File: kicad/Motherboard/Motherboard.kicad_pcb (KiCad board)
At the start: 2 copper layers, 64 parts, among them J1 USB_C_Receptacle_USB2.0, J2 Conn_01x16_Pin, J3 Conn_01x16_Pin, J4 Conn_01x16_Pin, J5 Conn_01x02_Pin, J6 Conn_01x04_Pin, J7 Conn_01x04_Pin, J8 Conn_01x16_Pin, J9 Conn_01x02_Pin, Q1 DMN3404L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

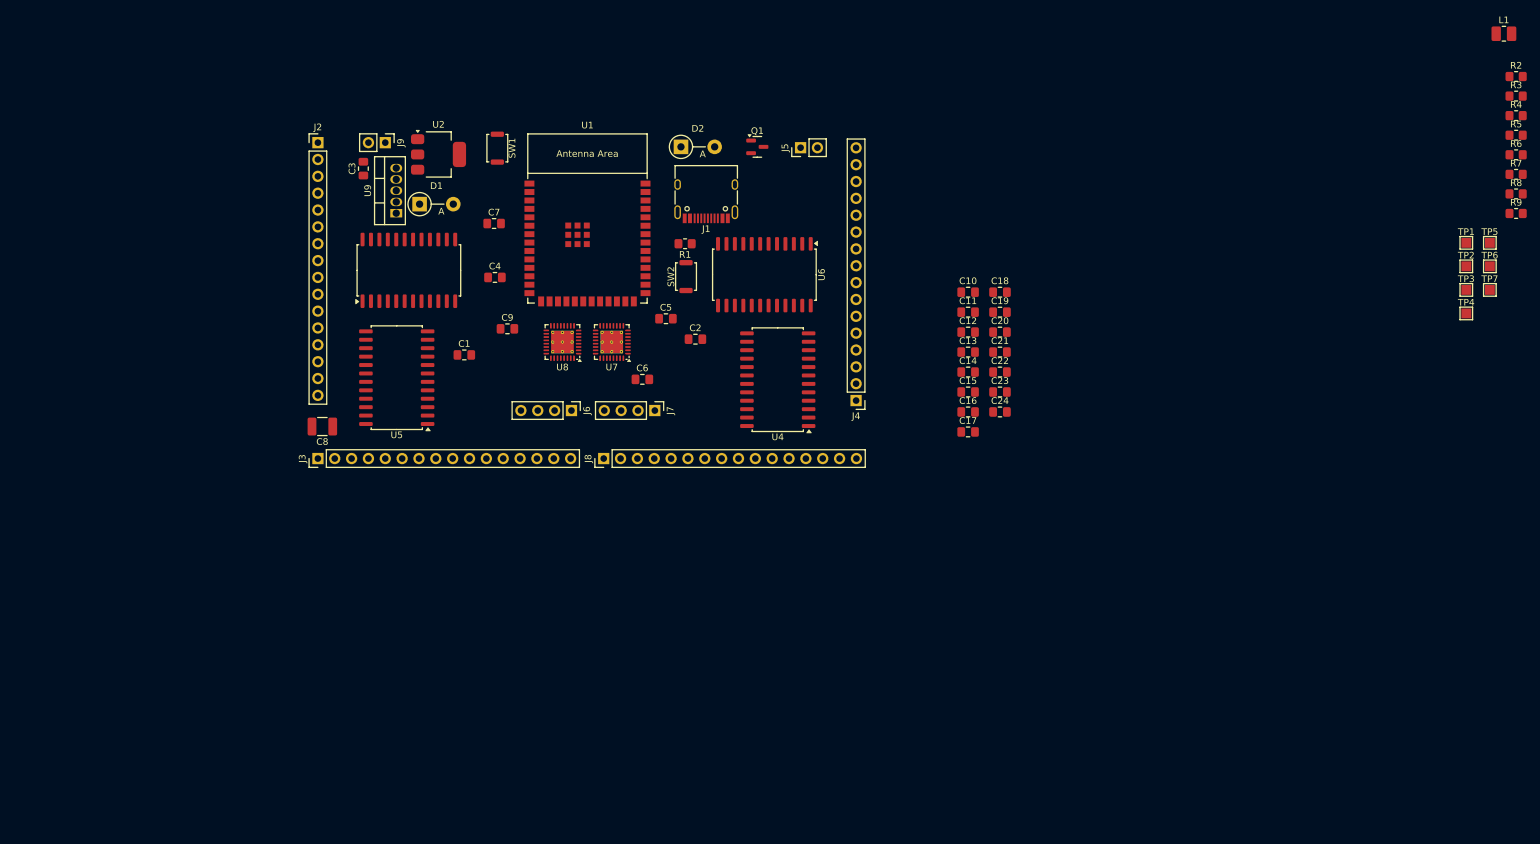
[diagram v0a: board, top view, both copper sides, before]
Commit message: Almost done - going to do a few more changes before I run the auto connector
We may want to manually add them tho cus apple is going to look at it...
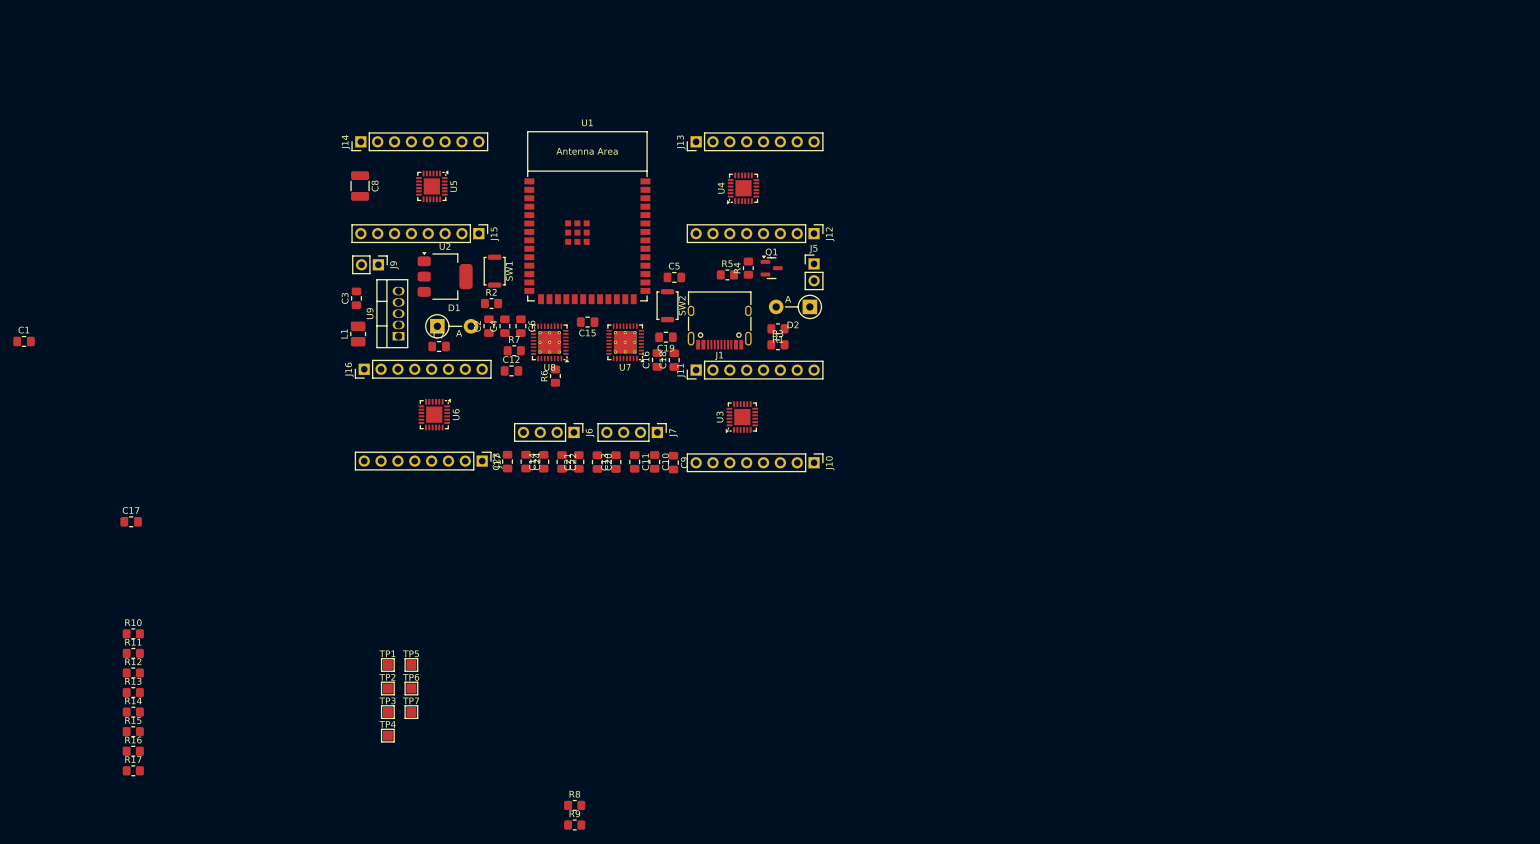
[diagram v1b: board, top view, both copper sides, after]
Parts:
- removed J2, J3, J4, J8: Conn_01x16_Pin, Connector_PinHeader_2.54mm:PinHeader_1x16_P2.54mm_Vertical
- added J10: Conn_01x08_Pin, Connector_PinHeader_2.54mm:PinHeader_1x08_P2.54mm_Vertical, F.Cu at (154.3, 129.5)
- added J11: Conn_01x08_Pin, Connector_PinHeader_2.54mm:PinHeader_1x08_P2.54mm_Vertical, F.Cu at (136.5, 115.6)
- added J12: Conn_01x08_Pin, Connector_PinHeader_2.54mm:PinHeader_1x08_P2.54mm_Vertical, F.Cu at (154.3, 95.0)
- added J13: Conn_01x08_Pin, Connector_PinHeader_2.54mm:PinHeader_1x08_P2.54mm_Vertical, F.Cu at (136.5, 81.2)
- added J14: Conn_01x08_Pin, Connector_PinHeader_2.54mm:PinHeader_1x08_P2.54mm_Vertical, F.Cu at (86.0, 81.2)
- added J15: Conn_01x08_Pin, Connector_PinHeader_2.54mm:PinHeader_1x08_P2.54mm_Vertical, F.Cu at (103.8, 95.0)
- added J16: Conn_01x08_Pin, Connector_PinHeader_2.54mm:PinHeader_1x08_P2.54mm_Vertical, F.Cu at (86.5, 115.4)
- added J17: Conn_01x08_Pin, Connector_PinHeader_2.54mm:PinHeader_1x08_P2.54mm_Vertical, F.Cu at (104.3, 129.3)
- added R10: 10k, Resistor_SMD:R_0805_2012Metric_Pad1.20x1.40mm_HandSolder, F.Cu at (51.7, 155.3)
- added R11: 10k, Resistor_SMD:R_0805_2012Metric_Pad1.20x1.40mm_HandSolder, F.Cu at (51.7, 158.3)
- added R12: 10k, Resistor_SMD:R_0805_2012Metric_Pad1.20x1.40mm_HandSolder, F.Cu at (51.7, 161.2)
- added R13: 10k, Resistor_SMD:R_0805_2012Metric_Pad1.20x1.40mm_HandSolder, F.Cu at (51.7, 164.2)
- added R14: 10k, Resistor_SMD:R_0805_2012Metric_Pad1.20x1.40mm_HandSolder, F.Cu at (51.7, 167.1)
- added R15: 10k, Resistor_SMD:R_0805_2012Metric_Pad1.20x1.40mm_HandSolder, F.Cu at (51.7, 170.1)
- added R16: 10k, Resistor_SMD:R_0805_2012Metric_Pad1.20x1.40mm_HandSolder, F.Cu at (51.7, 173.0)
- added R17: 10k, Resistor_SMD:R_0805_2012Metric_Pad1.20x1.40mm_HandSolder, F.Cu at (51.7, 176.0)
- U3, U4, U5, U6: value CD74HC4067M -> TCA9535RTWR; footprint Package_SO:SOIC-24W_7.5x15.4mm_P1.27mm -> Package_DFN_QFN:WQFN-24-1EP_4x4mm_P0.5mm_EP2.45x2.45mm
- moved L1 178.6 mm to (85.6, 110.1), turned to 90 degrees
- moved TP5 174.6 mm to (93.6, 160.0)
- moved TP6 174.6 mm to (93.6, 163.6)
- moved TP7 174.6 mm to (93.6, 167.1)
- moved TP1 174.6 mm to (90.0, 160.0)
- moved TP2 174.6 mm to (90.0, 163.6)
- moved TP3 174.6 mm to (90.0, 167.1)
- moved TP4 174.6 mm to (90.0, 170.7)
- moved R8 169.2 mm to (118.2, 181.2)
- moved R9 169.2 mm to (118.2, 184.2)
- moved R2 158.2 mm to (105.7, 105.5)
- moved R7 153.4 mm to (109.1, 112.6)
- moved R6 148.6 mm to (115.3, 116.5), turned to 90 degrees
- moved C17 126.9 mm to (51.3, 138.4)
- moved R5 120.8 mm to (141.2, 101.2)
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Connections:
- C2 pad 2: +3.3V -> SDA
- C4 pad 2: +3.3V -> SDA
- C6 pad 1: +3.3V -> SDA
- R2 pad 1: +3.3V -> SDA
- TP5 pad 1: +3.3V -> SDA
- U1 pad 12: COM1 -> unconnected-(U1-GPIO8/TOUCH8/ADC1_CH7-Pad12)
- U1 pad 15: bit2 -> unconnected-(U1-GPIO3/TOUCH3/ADC1_CH2-Pad15)
- U1 pad 17: EN2 -> unconnected-(U1-GPIO9/TOUCH9/ADC1_CH8/FSPIHD-Pad17)
- U1 pad 18: COM2 -> unconnected-(U1-GPIO10/TOUCH10/ADC1_CH9/FSPICS0/FSPIIO4-Pad18)
- U1 pad 19: EN3 -> unconnected-(U1-GPIO11/TOUCH11/ADC2_CH0/FSPID/FSPIIO5-Pad19)
- U1 pad 2: +3.3V -> SDA
- U1 pad 20: COM3 -> unconnected-(U1-GPIO12/TOUCH12/ADC2_CH1/FSPICLK/FSPIIO6-Pad20)
- U1 pad 38: bit1 -> SCL
- U1 pad 39: bit0 -> SDA
- U1 pad 4: bit3 -> unconnected-(U1-GPIO4/TOUCH4/ADC1_CH3-Pad4)
- U1 pad 5: EN0 -> unconnected-(U1-GPIO5/TOUCH5/ADC1_CH4-Pad5)
- U1 pad 6: COM0 -> unconnected-(U1-GPIO6/TOUCH6/ADC1_CH5-Pad6)
- U1 pad 7: EN1 -> unconnected-(U1-GPIO7/TOUCH7/ADC1_CH6-Pad7)
- U2 pad 2: +3.3V -> SDA
- U3 pad 1: COM0 -> Net-(J10-Pin_8)
- U3 pad 10: bit0 -> Net-(J11-Pin_8)
- U3 pad 11: bit1 -> Net-(J11-Pin_7)
- U3 pad 12: GND -> Net-(J11-Pin_6)
- U3 pad 13: bit3 -> Net-(J11-Pin_5)
- U3 pad 14: bit2 -> Net-(J11-Pin_4)
- U3 pad 15: EN0 -> Net-(J11-Pin_3)
- U3 pad 18: Net-(J2-Pin_3) -> GND
- U3 pad 19: Net-(J2-Pin_4) -> SCL
- U3 pad 20: Net-(J2-Pin_5) -> SDA
- U3 pad 21: Net-(J2-Pin_6) -> SDA
- U3 pad 22: Net-(J2-Pin_7) -> unconnected-(U3-~{INT}-Pad22)
- U3 pad 23: Net-(J2-Pin_8) -> GND
- U3 pad 24: +5V -> GND
- U3 pad 9: Net-(J2-Pin_16) -> GND
- U4 pad 1: COM1 -> Net-(J12-Pin_8)
- U4 pad 10: bit0 -> Net-(J13-Pin_8)
- U4 pad 11: bit1 -> Net-(J13-Pin_7)
- U4 pad 12: GND -> Net-(J13-Pin_6)
- U4 pad 13: bit3 -> Net-(J13-Pin_5)
- U4 pad 14: bit2 -> Net-(J13-Pin_4)
- U4 pad 15: EN1 -> Net-(J13-Pin_3)
- U4 pad 18: Net-(J8-Pin_3) -> GND
- U4 pad 19: Net-(J8-Pin_4) -> SCL
- U4 pad 20: Net-(J8-Pin_5) -> SDA
- U4 pad 21: Net-(J8-Pin_6) -> SDA
- U4 pad 22: Net-(J8-Pin_7) -> unconnected-(U4-~{INT}-Pad22)
- U4 pad 23: Net-(J8-Pin_8) -> GND
- U4 pad 24: +5V -> SDA
- U4 pad 9: Net-(J8-Pin_16) -> GND
- U5 pad 1: COM2 -> Net-(J14-Pin_8)
- U5 pad 10: bit0 -> Net-(J15-Pin_8)
- U5 pad 11: bit1 -> Net-(J15-Pin_7)
- U5 pad 12: GND -> Net-(J15-Pin_6)
- U5 pad 13: bit3 -> Net-(J15-Pin_5)
- U5 pad 14: bit2 -> Net-(J15-Pin_4)
- U5 pad 15: EN2 -> Net-(J15-Pin_3)
- U5 pad 18: Net-(J3-Pin_3) -> GND
- U5 pad 19: Net-(J3-Pin_4) -> SCL
- U5 pad 20: Net-(J3-Pin_5) -> SDA
- U5 pad 21: Net-(J3-Pin_6) -> SDA
- U5 pad 22: Net-(J3-Pin_7) -> unconnected-(U5-~{INT}-Pad22)
- U5 pad 23: Net-(J3-Pin_8) -> SDA
- U5 pad 24: +5V -> GND
- U5 pad 9: Net-(J3-Pin_16) -> GND
- U6 pad 1: COM3 -> Net-(J16-Pin_8)
- U6 pad 10: bit0 -> Net-(J17-Pin_8)
- U6 pad 11: bit1 -> Net-(J17-Pin_7)
- U6 pad 12: GND -> Net-(J17-Pin_6)
- U6 pad 13: bit3 -> Net-(J17-Pin_5)
- U6 pad 14: bit2 -> Net-(J17-Pin_4)
- U6 pad 15: EN3 -> Net-(J17-Pin_3)
- U6 pad 18: Net-(J4-Pin_3) -> SDA
- U6 pad 19: Net-(J4-Pin_4) -> SCL
- U6 pad 20: Net-(J4-Pin_5) -> SDA
- U6 pad 21: Net-(J4-Pin_6) -> SDA
- U6 pad 22: Net-(J4-Pin_7) -> unconnected-(U6-~{INT}-Pad22)
- U6 pad 23: Net-(J4-Pin_8) -> GND
- U6 pad 24: +5V -> GND
- U6 pad 9: Net-(J4-Pin_16) -> GND
- U7 pad 15: +3.3V -> SDA
- U8 pad 15: +3.3V -> SDA

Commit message: updated layout
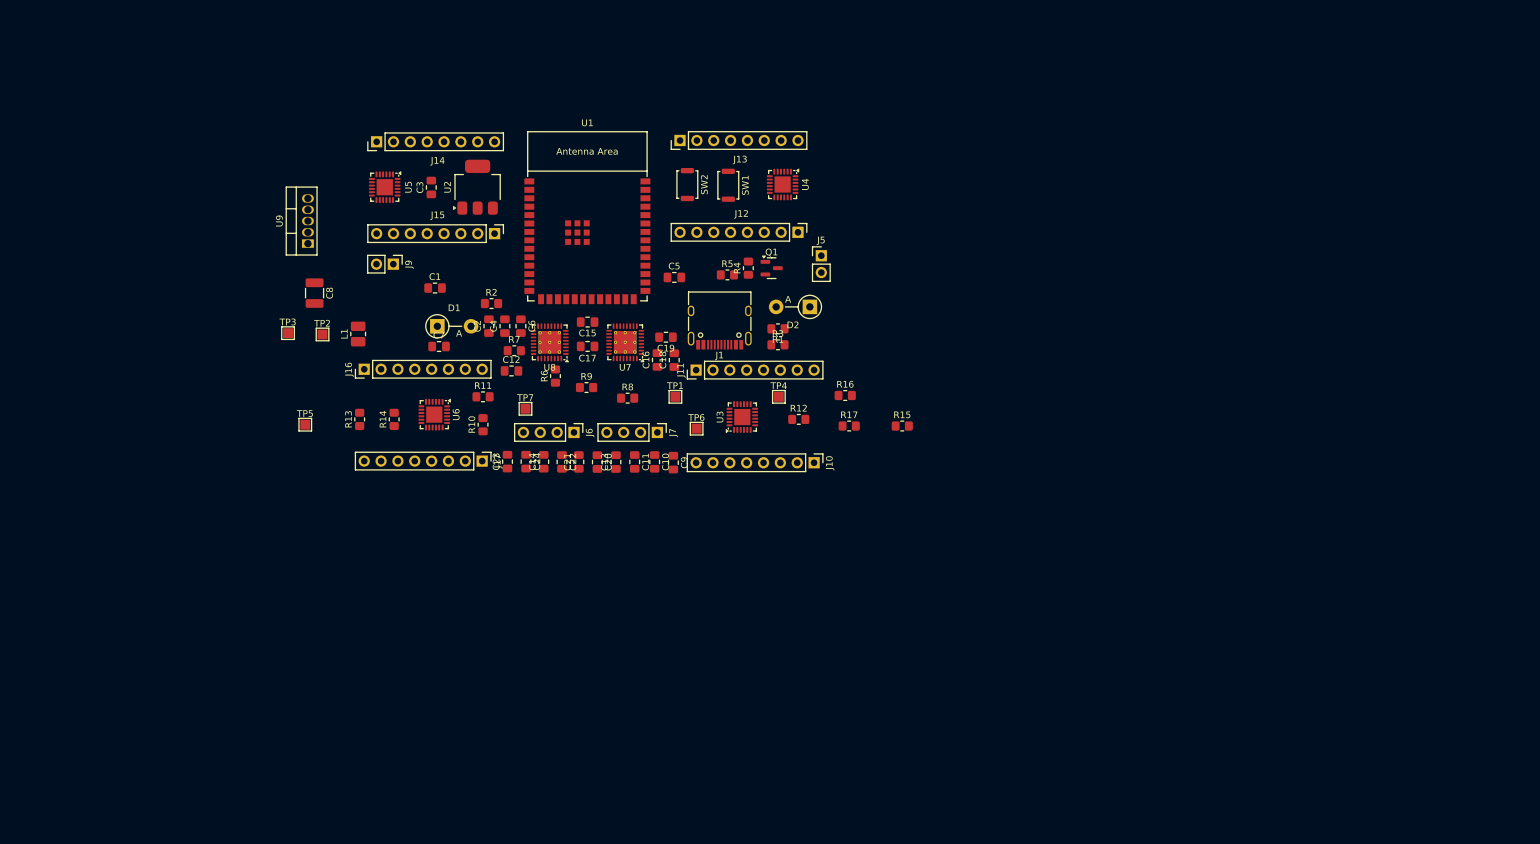
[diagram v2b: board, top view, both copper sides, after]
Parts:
- moved R15 124.8 mm to (167.6, 124.0)
- moved R16 120.0 mm to (159.0, 119.4)
- moved R17 119.8 mm to (159.6, 124.0)
- moved R12 107.4 mm to (152.0, 123.0)
- moved TP4 78.0 mm to (149.0, 119.6)
- moved C17 73.7 mm to (120.2, 112.0)
- moved R9 66.0 mm to (120.0, 118.2)
- moved R11 65.4 mm to (104.4, 119.6)
- moved C1 62.5 mm to (97.2, 103.2)
- moved R8 61.9 mm to (126.2, 119.8)
- moved R10 61.4 mm to (104.4, 123.8), turned to 90 degrees
- moved TP1 59.3 mm to (133.4, 119.6)
- moved R14 59.1 mm to (91.0, 123.0), turned to 90 degrees
- moved TP3 59.1 mm to (75.0, 110.0)
- moved TP6 58.2 mm to (136.6, 124.4)
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
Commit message: Gode
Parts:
- moved TP4 78.0 mm to (90.0, 170.7)
- moved TP5 69.4 mm to (132.2, 81.0)
- moved TP6 51.0 mm to (92.3, 99.1)
- moved R15 50.3 mm to (117.3, 125.1), turned to -90 degrees
- moved R17 48.2 mm to (111.4, 125.1), turned to -90 degrees
- moved R16 45.0 mm to (114.4, 125.1), turned to -90 degrees
- moved R10 44.8 mm to (132.2, 88.7), turned to -90 degrees
- moved TP1 39.6 mm to (94.5, 112.0)
- moved R13 37.5 mm to (123.2, 125.1), turned to -90 degrees
- moved SW1 36.3 mm to (105.1, 86.2), turned to 0 degrees
- moved R14 29.3 mm to (120.3, 125.1), turned to -90 degrees
- moved R12 25.9 mm to (126.2, 125.1), turned to -90 degrees
- moved TP3 25.7 mm to (73.5, 135.6)
- moved R11 25.3 mm to (129.1, 125.1), turned to -90 degrees
- moved C3 20.2 mm to (85.3, 104.8)
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
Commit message: re-render layout
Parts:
- removed TP3: BeforeEM_TestPoint, TestPoint:TestPoint_Pad_1.5x1.5mm
- moved TP4 48.8 mm to (105.4, 124.4)
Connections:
- C1 pad 1: GND -> +3.3V
- C10 pad 2: GND -> +3.3V
- C11 pad 2: GND -> +3.3V
- C13 pad 1: GND -> +3.3V
- C14 pad 1: GND -> +3.3V
- C15 pad 1: GND -> +3.3V
- C19 pad 1: GND -> +3.3V
- C2 pad 1: GND -> +3.3V
- C2 pad 2: SDA -> +3.3V
- C20 pad 2: GND -> +3.3V
- C21 pad 1: GND -> +3.3V
- C22 pad 2: GND -> +3.3V
- C23 pad 1: GND -> +3.3V
- C24 pad 2: GND -> +3.3V
- C3 pad 2: GND -> +3.3V
- C4 pad 1: GND -> +3.3V
- C4 pad 2: SDA -> +3.3V
- C5 pad 2: GND -> +3.3V
- C6 pad 1: SDA -> +3.3V
- C6 pad 2: GND -> +3.3V
- C7 pad 2: GND -> +3.3V
- C8 pad 2: GND -> +3.3V
- C9 pad 2: GND -> +3.3V
- D1 pad 2: GND -> +3.3V
- J1 pad A1: GND -> +3.3V
- J1 pad A12: GND -> +3.3V
- J1 pad B1: GND -> +3.3V
- J1 pad B12: GND -> +3.3V
- J1 pad S1: GND -> +3.3V
- J9 pad 2: GND -> +3.3V
- Q1 pad 2: GND -> +3.3V
- R1 pad 1: GND -> +3.3V
- R10 pad 1: SDA -> +3.3V
- R11 pad 1: SDA -> +3.3V
- R12 pad 1: SDA -> +3.3V
- R12 pad 2: SDA -> SCL
- R13 pad 1: SDA -> +3.3V
- R13 pad 2: SDA -> SCL
- R14 pad 1: SDA -> +3.3V
- R15 pad 1: SDA -> +3.3V
- R15 pad 2: SDA -> SCL
- R16 pad 1: SDA -> +3.3V
- R17 pad 1: SDA -> +3.3V
- R17 pad 2: SDA -> SCL
- R2 pad 1: SDA -> +3.3V
- R3 pad 2: GND -> +3.3V
- R5 pad 1: GND -> +3.3V
- R6 pad 1: GND -> +3.3V
- R7 pad 1: GND -> +3.3V
- R8 pad 1: GND -> +3.3V
- R9 pad 1: GND -> +3.3V
- SW1 pad 1: GND -> +3.3V
- SW2 pad 2: GND -> +3.3V
- TP4 pad 1: GND -> +3.3V
- TP5 pad 1: SDA -> +3.3V
- U1 pad 1: GND -> +3.3V
- U1 pad 10: STEP_1 -> unconnected-(U1-GPIO17/U1TXD/ADC2_CH6/DAC_1-Pad10)
- U1 pad 11: UART_1 -> unconnected-(U1-GPIO18/U1RXD/ADC2_CH7/DAC_2/CLK_OUT3-Pad11)
- U1 pad 13: unconnected-(U1-GPIO19/U1RTS/ADC2_CH8/CLK_OUT2/USB_D--Pad13) -> /D-
- U1 pad 14: unconnected-(U1-GPIO20/U1CTS/ADC2_CH9/CLK_OUT1/USB_D+-Pad14) -> /D+
- U1 pad 15: unconnected-(U1-GPIO3/TOUCH3/ADC1_CH2-Pad15) -> STEP_1
- U1 pad 18: unconnected-(U1-GPIO10/TOUCH10/ADC1_CH9/FSPICS0/FSPIIO4-Pad18) -> MAGCT
- U1 pad 2: SDA -> +3.3V
- U1 pad 21: ENN_1 -> unconnected-(U1-GPIO13/TOUCH13/ADC2_CH2/FSPIQ/FSPIIO7-Pad21)
- U1 pad 22: DIR_1 -> unconnected-(U1-GPIO14/TOUCH14/ADC2_CH3/FSPIWP/FSPIDQS-Pad22)
- U1 pad 23: ENN_2 -> unconnected-(U1-GPIO21-Pad23)
- U1 pad 24: DIR_2 -> SCL
- U1 pad 25: STEP_2 -> SCL
- U1 pad 28: UART_2 -> unconnected-(U1-SPIIO6/GPIO35/FSPID-Pad28)
- U1 pad 29: MAGCT -> unconnected-(U1-SPIIO7/GPIO36/FSPICLK-Pad29)
- U1 pad 36: unconnected-(U1-U0RXD/GPIO44/CLK_OUT2-Pad36) -> UART_1
- U1 pad 37: unconnected-(U1-U0TXD/GPIO43/CLK_OUT1-Pad37) -> UART_2
- U1 pad 38: SCL -> DIR_1
- U1 pad 39: SDA -> ENN_1
- U1 pad 4: unconnected-(U1-GPIO4/TOUCH4/ADC1_CH3-Pad4) -> ENN_2
- U1 pad 40: GND -> +3.3V
- U1 pad 41: GND -> +3.3V
- U1 pad 5: unconnected-(U1-GPIO5/TOUCH5/ADC1_CH4-Pad5) -> DIR_2
- U1 pad 6: unconnected-(U1-GPIO6/TOUCH6/ADC1_CH5-Pad6) -> STEP_2
- U2 pad 1: GND -> +3.3V
- U2 pad 2: SDA -> +3.3V
- U3 pad 18: GND -> +3.3V
- U3 pad 20: SDA -> SCL
- U3 pad 21: SDA -> +3.3V
- U3 pad 23: GND -> +3.3V
- U3 pad 24: GND -> +3.3V
- U3 pad 25: GND -> +3.3V
- U3 pad 9: GND -> +3.3V
- U4 pad 18: GND -> +3.3V
- U4 pad 20: SDA -> SCL
- U4 pad 21: SDA -> +3.3V
- U4 pad 23: GND -> +3.3V
- U4 pad 24: SDA -> +3.3V
- U4 pad 25: GND -> +3.3V
- U4 pad 9: GND -> +3.3V
- U5 pad 18: GND -> +3.3V
- U5 pad 20: SDA -> SCL
- U5 pad 21: SDA -> +3.3V
- U5 pad 23: SDA -> +3.3V
- U5 pad 24: GND -> +3.3V
- U5 pad 25: GND -> +3.3V
- U5 pad 9: GND -> +3.3V
- U6 pad 18: SDA -> +3.3V
- U6 pad 20: SDA -> SCL
- U6 pad 21: SDA -> +3.3V
- U6 pad 23: GND -> +3.3V
- U6 pad 24: GND -> +3.3V
- U6 pad 25: GND -> +3.3V
- U6 pad 9: GND -> +3.3V
- U7 pad 15: SDA -> +3.3V
- U7 pad 18: GND -> +3.3V
- U7 pad 3: GND -> +3.3V
- U8 pad 15: SDA -> +3.3V
- U8 pad 18: GND -> +3.3V
- U8 pad 3: GND -> +3.3V
- U9 pad 3: GND -> +3.3V
- U9 pad 5: GND -> +3.3V

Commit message: fixed schematic
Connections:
- C1 pad 1: +3.3V -> GND
- C10 pad 2: +3.3V -> GND
- C11 pad 2: +3.3V -> GND
- C13 pad 1: +3.3V -> GND
- C14 pad 1: +3.3V -> GND
- C15 pad 1: +3.3V -> GND
- C19 pad 1: +3.3V -> GND
- C2 pad 1: +3.3V -> GND
- C20 pad 2: +3.3V -> GND
- C21 pad 1: +3.3V -> GND
- C22 pad 2: +3.3V -> GND
- C23 pad 1: +3.3V -> GND
- C24 pad 2: +3.3V -> GND
- C3 pad 2: +3.3V -> GND
- C4 pad 1: +3.3V -> GND
- C5 pad 2: +3.3V -> GND
- C6 pad 2: +3.3V -> GND
- C7 pad 2: +3.3V -> GND
- C8 pad 2: +3.3V -> GND
- C9 pad 2: +3.3V -> GND
- D1 pad 2: +3.3V -> GND
- J1 pad A1: +3.3V -> GND
- J1 pad A12: +3.3V -> GND
- J1 pad B1: +3.3V -> GND
- J1 pad B12: +3.3V -> GND
- J1 pad S1: +3.3V -> GND
- J9 pad 2: +3.3V -> GND
- Q1 pad 2: +3.3V -> GND
- R1 pad 1: +3.3V -> GND
- R12 pad 2: SCL -> SDA
- R13 pad 2: SCL -> SDA
- R15 pad 2: SCL -> SDA
- R17 pad 2: SCL -> SDA
- R3 pad 2: +3.3V -> GND
- R5 pad 1: +3.3V -> GND
- R6 pad 1: +3.3V -> GND
- R7 pad 1: +3.3V -> GND
- R8 pad 1: +3.3V -> GND
- R9 pad 1: +3.3V -> GND
- SW1 pad 1: +3.3V -> GND
- SW2 pad 2: +3.3V -> GND
- TP4 pad 1: +3.3V -> GND
- U1 pad 1: +3.3V -> GND
- U1 pad 24: SCL -> SDA
- U1 pad 40: +3.3V -> GND
- U1 pad 41: +3.3V -> GND
- U2 pad 1: +3.3V -> GND
- U3 pad 18: +3.3V -> GND
- U3 pad 20: SCL -> SDA
- U3 pad 23: +3.3V -> GND
- U3 pad 24: +3.3V -> GND
- U3 pad 25: +3.3V -> GND
- U3 pad 9: +3.3V -> GND
- U4 pad 18: +3.3V -> GND
- U4 pad 20: SCL -> SDA
- U4 pad 23: +3.3V -> GND
- U4 pad 25: +3.3V -> GND
- U4 pad 9: +3.3V -> GND
- U5 pad 18: +3.3V -> GND
- U5 pad 20: SCL -> SDA
- U5 pad 24: +3.3V -> GND
- U5 pad 25: +3.3V -> GND
- U5 pad 9: +3.3V -> GND
- U6 pad 20: SCL -> SDA
- U6 pad 23: +3.3V -> GND
- U6 pad 24: +3.3V -> GND
- U6 pad 25: +3.3V -> GND
- U6 pad 9: +3.3V -> GND
- U7 pad 18: +3.3V -> GND
- U7 pad 3: +3.3V -> GND
- U8 pad 18: +3.3V -> GND
- U8 pad 3: +3.3V -> GND
- U9 pad 3: +3.3V -> GND
- U9 pad 5: +3.3V -> GND
